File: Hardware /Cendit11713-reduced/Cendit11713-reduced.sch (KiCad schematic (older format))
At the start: 2 parts, among them U1 PIC18F45K50-X/MV

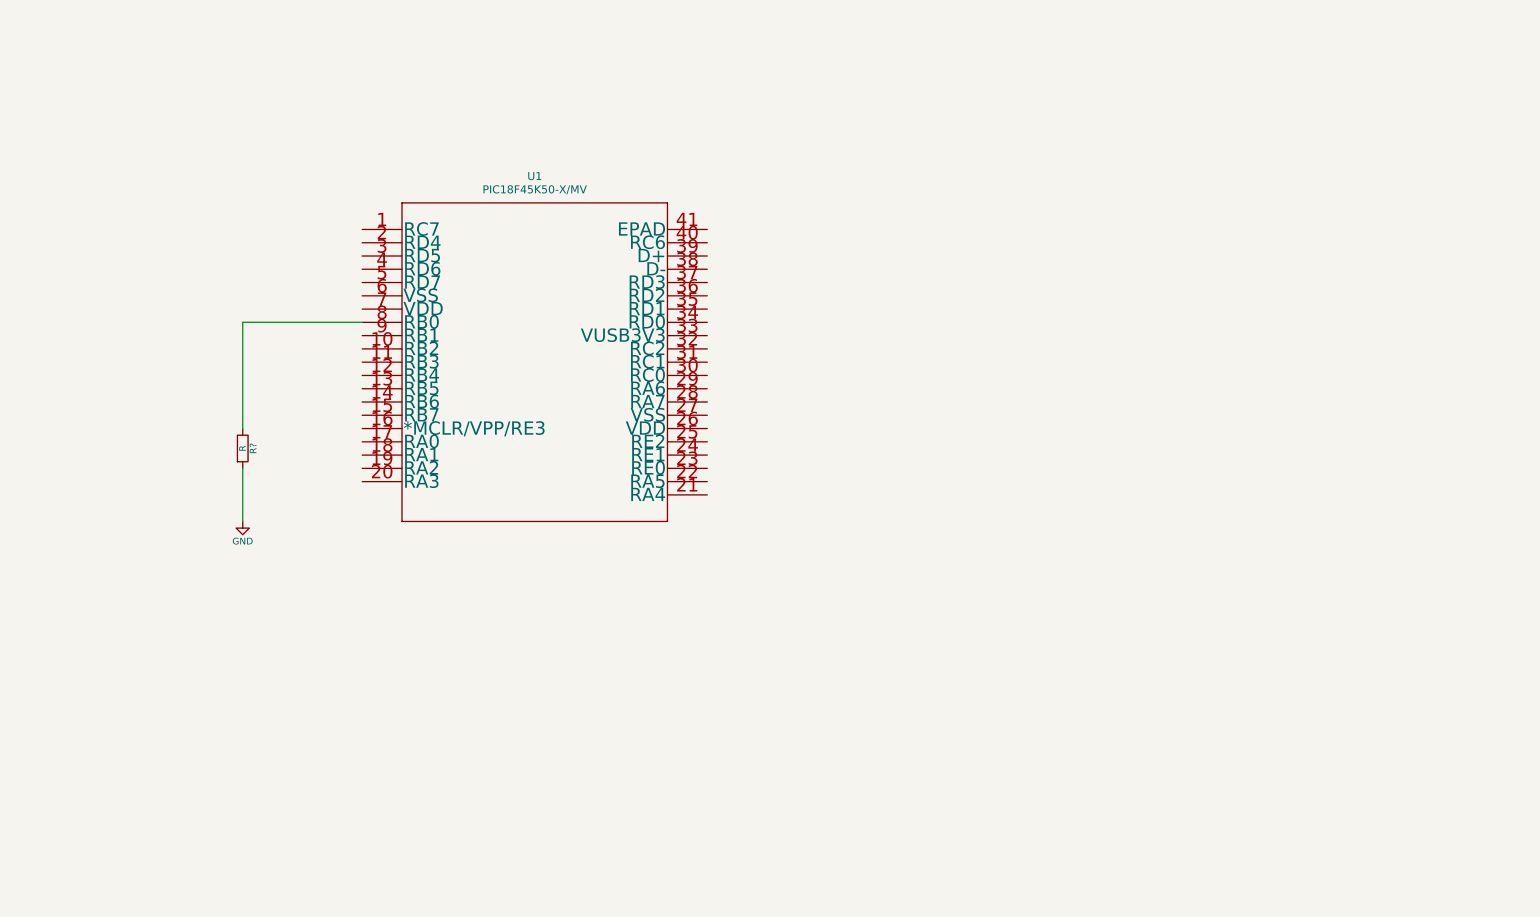
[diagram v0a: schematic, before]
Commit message: Edicion de esquematicos CenditBoard
  - Version reducida CenditBoard 11713
  - Configuracion y edicion con Kicad
  - Actualizada libreria de componentes
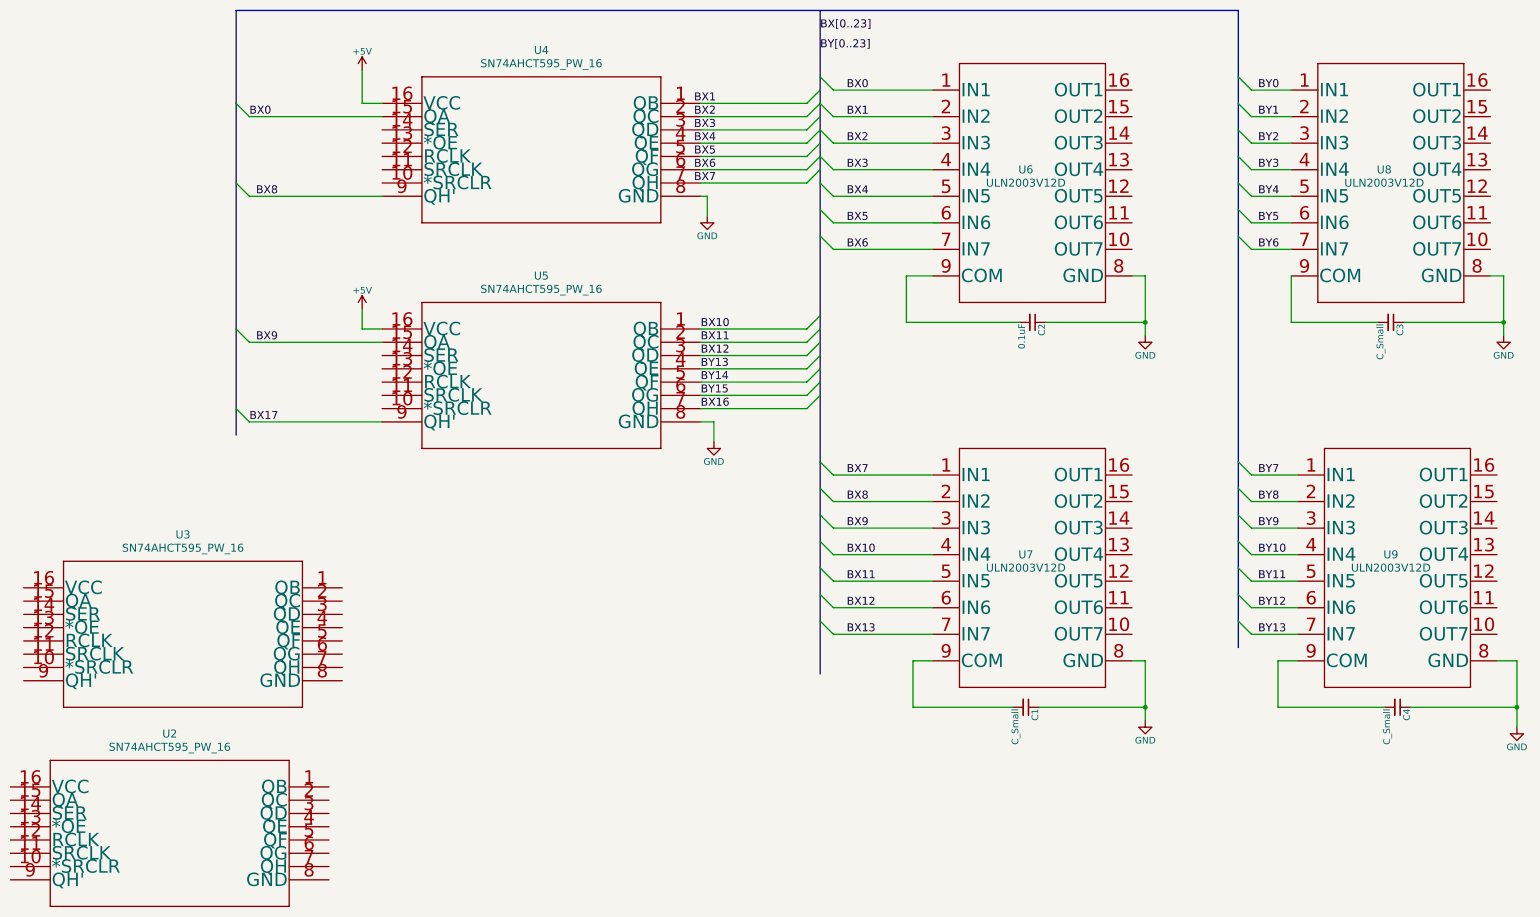
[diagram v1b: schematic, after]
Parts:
- removed R?: R, symbol R
- removed U1: PIC18F45K50-X/MV, UQFN40_5X5MC, symbol PIC18F45K50-X/MV
- added C1, C3, C4: C_Small, symbol C_Small
- added C2: 0.1uF, symbol C_Small
- added U2, U3, U4, U5: SN74AHCT595_PW_16, LibreriaCendit:SN74AHCT595_PW_16, symbol SN74AHCT595_PW_16
- added U6, U7, U8, U9: ULN2003V12D, LibreriaCendit:ULN2003V12DR, symbol ULN2003V12D
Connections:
- net GND: now also C1.1, C2.1, C3.1, C4.1, U4.8 (GND), U5.8 (GND), U6.8 (GND), U7.8 (GND), U8.8 (GND), U9.8 (GND)
- new net: C3.2, U8.9 (COM)
- new net: C2.2, U6.9 (COM)
- new net: C4.2, U9.9 (COM)
- new net: C1.2, U7.9 (COM)
- new net +5V: U4.16 (VCC), U5.16 (VCC)
- new net BX0: U4.15 (QA), U6.1 (IN1)
- new net BX1: U6.2 (IN2)
- new net BX10: U5.1 (QB), U7.4 (IN4)
- new net BX11: U5.2 (QC), U7.5 (IN5)
- new net BX12: U5.3 (QD), U7.6 (IN6)
- new net BX13: U7.7 (IN7)
- new net BX16: U5.7 (QH)
- new net BX17: U5.9 (QH')
- new net BX2: U6.3 (IN3)
- new net BX3: U6.4 (IN4)
- new net BX4: U6.5 (IN5)
- new net BX6: U6.7 (IN7)
- new net BX7: U7.1 (IN1)
- new net BX8: U4.9 (QH'), U7.2 (IN2)
- new net BX9: U5.15 (QA), U7.3 (IN3)
- new net BY0: U8.1 (IN1)
- new net BY1: U8.2 (IN2)
- new net BY10: U9.4 (IN4)
- new net BY11: U9.5 (IN5)
- new net BY12: U9.6 (IN6)
- new net BY13: U5.4 (QE), U9.7 (IN7)
- new net BY14: U5.5 (QF)
- new net BY15: U5.6 (QG)
- new net BY2: U8.3 (IN3)
- new net BY3: U8.4 (IN4)
- new net BY4: U8.5 (IN5)
- new net BY5: U8.6 (IN6)
- new net BY6: U8.7 (IN7)
- new net BY7: U9.1 (IN1)
- new net BY8: U9.2 (IN2)
- new net BY9: U9.3 (IN3)
